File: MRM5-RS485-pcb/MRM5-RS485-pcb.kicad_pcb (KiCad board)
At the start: 2 copper layers, 50.2 x 25 mm, 75 parts, among them IC1 ADPL16000AATA+T, IC2 REF35160QDBVR, J1 Conn_01x05, J2 Conn_01x02, J3 Conn_01x02, J4 Conn_01x02, J5 GSB1C41110SSHR, J6 Conn_01x02, U1 ADA4528-2ACPZ, U2 ADA4528-2ACPZ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

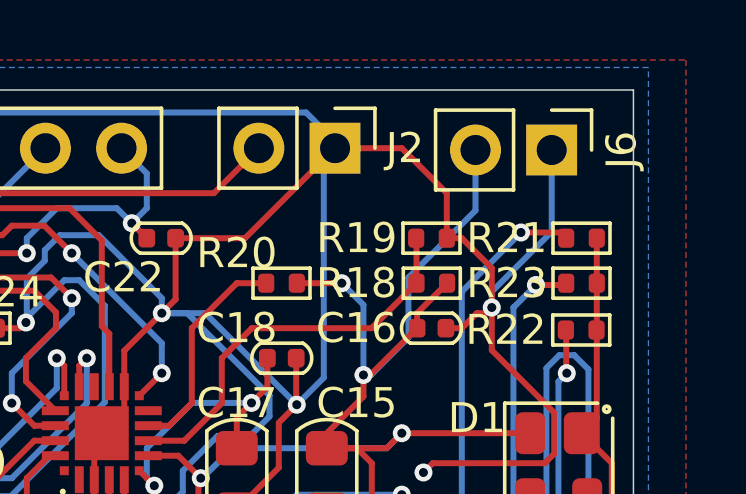
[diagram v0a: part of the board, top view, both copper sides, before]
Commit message: logo added on pcb
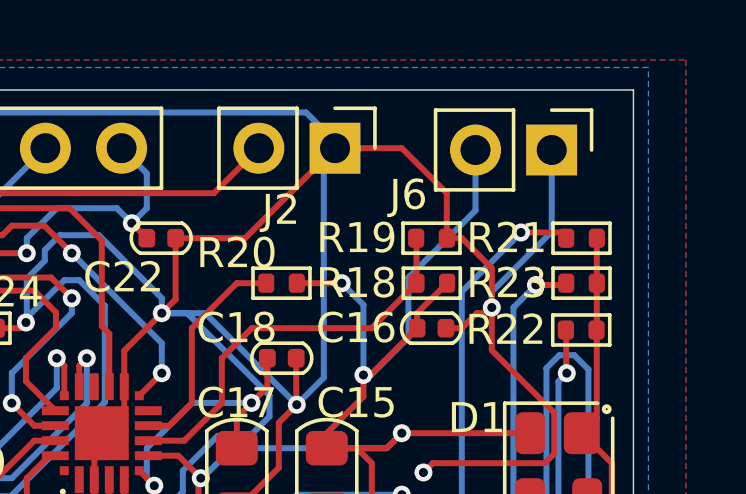
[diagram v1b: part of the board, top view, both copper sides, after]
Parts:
- added Symbol1: ktw07182@gmail.com, Mouser:ktw07182_logo, B.Cu at (176.0, 127.8)
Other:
- board text added: "MRM5"
- board text added: "v1.0.0"

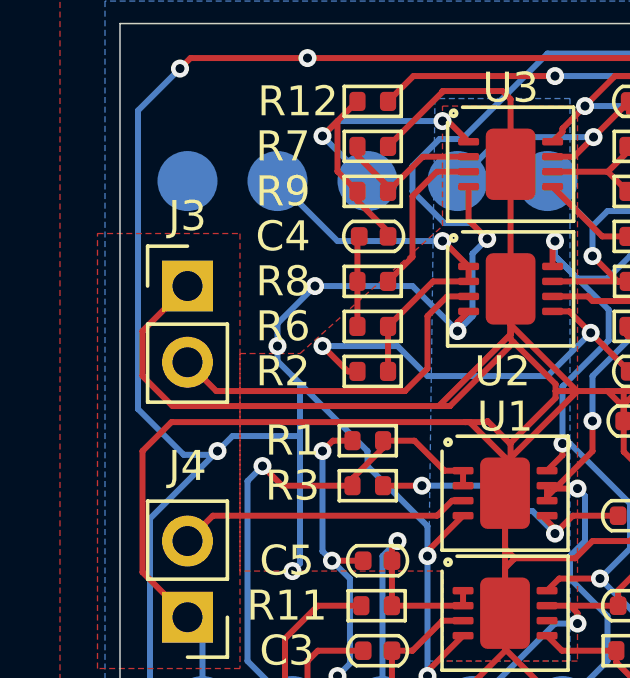
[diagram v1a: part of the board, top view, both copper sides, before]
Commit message: sensor is added
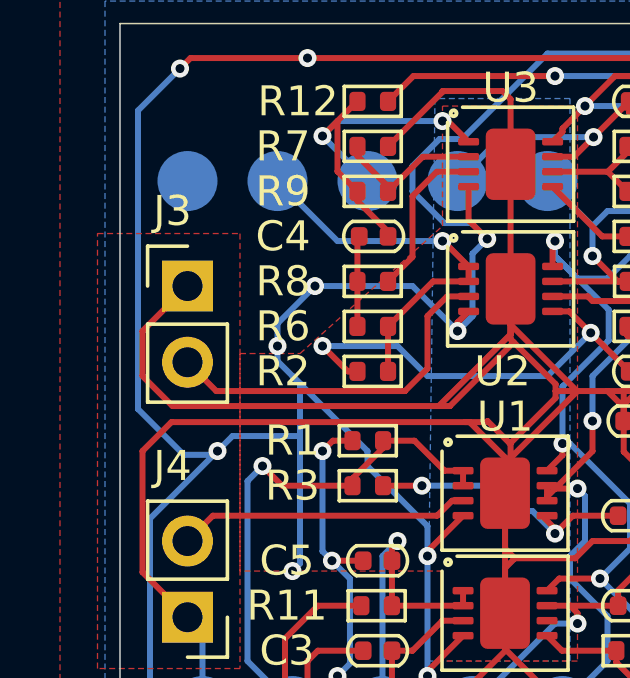
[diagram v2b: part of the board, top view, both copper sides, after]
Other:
- board text added: "- 5V +"
- board text added: "3V3 DIO CLK RST GND"
- board text added: "CT"
- board text added: "PT"
- board text added: "SYNC"
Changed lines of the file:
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@@
 		(tags "Through hole pin header THT 1x02 2.54mm single row")
 		(property "Reference" "J3"
-			(at 0 -2.33 0)
+			(at -0.5 -2.5 0)
 			(layer "F.SilkS")
 			(effects
@@
 		(tags "Through hole pin header THT 1x02 2.54mm single row")
 		(property "Reference" "J4"
-			(at 0 5.04 0)
+			(at 0.5 5.04 0)
 			(layer "F.SilkS")
 			(effects
@@
 		)
 	)
+	(gr_text "3V3 DIO CLK RST GND"
+		(at 196.75 118.75 0)
+		(layer "B.SilkS")
+		(effects
+			(font
+				(size 0.7 0.7)
+				(thickness 0.1)
+			)
+			(justify left bottom mirror)
+		)
+	)
 	(gr_text "V2"
 		(at 178.25 135.25 0)
@@
 		)
 	)
+	(gr_text "CT"
+		(at 168.25 124.75 -0)
+		(layer "B.SilkS")
+		(effects
+			(font
+				(size 0.7 0.7)
+				(thickness 0.1)
+			)
+			(justify left bottom mirror)
+		)
+	)
 	(gr_text "W_PW"
 		(at 207.25 138.25 0)
@@
 		)
 	)
+	(gr_text "PT"
+		(at 168.25 133 -0)
+		(layer "B.SilkS")
+		(effects
+			(font
+				(size 0.7 0.7)
+				(thickness 0.1)
+			)
+			(justify left bottom mirror)
+		)
+	)
 	(gr_text "Calibration"
 		(at 192 122 0)
@@
 		)
 	)
+	(gr_text "- 5V +"
+		(at 211 118.75 0)
+		(layer "B.SilkS")
+		(effects
+			(font
+				(size 0.7 0.7)
+				(thickness 0.1)
+			)
+			(justify left bottom mirror)
+		)
+	)
 	(gr_text "1V6"
 		(at 167 117.75 0)
@@
 				(thickness 0.1)
 			)
+			(justify left bottom mirror)
+		)
+	)
+	(gr_text "SYNC"
+		(at 203.25 118.75 -0)
+		(layer "B.SilkS")
+		(effects
+			(font
+				(size 0.7 0.7)
+				(thickness 0.1)
+			)
